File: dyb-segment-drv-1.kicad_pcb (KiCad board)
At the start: 2 copper layers, 76 x 76 mm, 192 parts, among them J1 Conn_01x10, Q1 HL2300, Q10 HL2300, Q11 HL2300, Q12 HL2300, Q13 HL2300, Q14 HL2300, Q15 HL2300, Q16 HL2300, Q2 HL2300, Q3 HL2300, Q4 HL2300, Q5 HL2300, Q6 HL2300, Q7 HL2300, Q8 HL2300, Q9 HL2300, SW1 SW_SPDT, U1 AP2112K-1.8, U10 74AUC2G32, U11 74AUC2G32, U12 74AUC2G32, U13 74AUC2G32, U14 74AUC2G32, U15 Inverter_Schmitt_Dual, U16 Inverter_Schmitt_Dual, U17 SN74AUP2G08, U18 SN74AUP2G08, U19 SN74AUP2G08, U2 GS3911AG, U20 SN74AUP2G08, U21 SN74AUP2G08, U22 74AUC2G32, U23 74AUC2G32, U24 74AUC2G32, U25 74AUC2G32, U26 74AUC2G32, U27 GS3911AG, U28 SN74AUP2G08, U29 SN74AUP2G08, U3 SN74AUP2G08, U30 SN74AUP2G08, U31 SN74AUP2G08, U32 SN74AUP2G08, U33 SN74AUP2G08, U34 74AUC2G32, U35 74AUC2G32, U36 74AUC2G32, U37 74AUC2G32, U38 74AUC2G32, U39 74AUC2G32, U4 SN74AUP2G08, U40 Inverter_Schmitt_Dual, U41 Inverter_Schmitt_Dual, U42 SN74AUP2G08, U43 SN74AUP2G08, U44 SN74AUP2G08, U45 SN74AUP2G08, U46 SN74AUP2G08, U47 74AUC2G32, U48 74AUC2G32, U49 74AUC2G32, U5 SN74AUP2G08, U50 74AUC2G32, U51 74AUC2G32, U6 SN74AUP2G08, U7 SN74AUP2G08, U8 SN74AUP2G08, U9 74AUC2G32

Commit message: pcb: add f routing
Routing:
- net /Segment Driver/~{D3}: track 110.0 -> 131.7 mm, vias 12 -> 17
- net /Segment Driver/~{D2}: track 81.4 -> 93.7 mm, vias 4 -> 8
- net Net-(U23-Pad3): track 0.00 -> 9.21 mm, vias 0 -> 2
- net Net-(U17-Pad3): track 0.00 -> 7.02 mm
- net /A2: track 85.7 -> 92.1 mm, vias 6 -> 8
- net /A0: track 69.6 -> 75.7 mm, vias 2 -> 4
- net /Segment Driver/~{D1}: track 90.5 -> 96.3 mm, vias 10 -> 12
- net Net-(U19-Pad7): track 0.00 -> 5.61 mm
- net Net-(U19-Pad3): track 0.00 -> 4.86 mm
- net Net-(U18-Pad7): track 0.00 -> 4.76 mm
- net Net-(U17-Pad7): track 0.00 -> 3.76 mm
- net Net-(U24-Pad6): track 0.00 -> 0.50 mm
- net GND: vias 0 -> 49

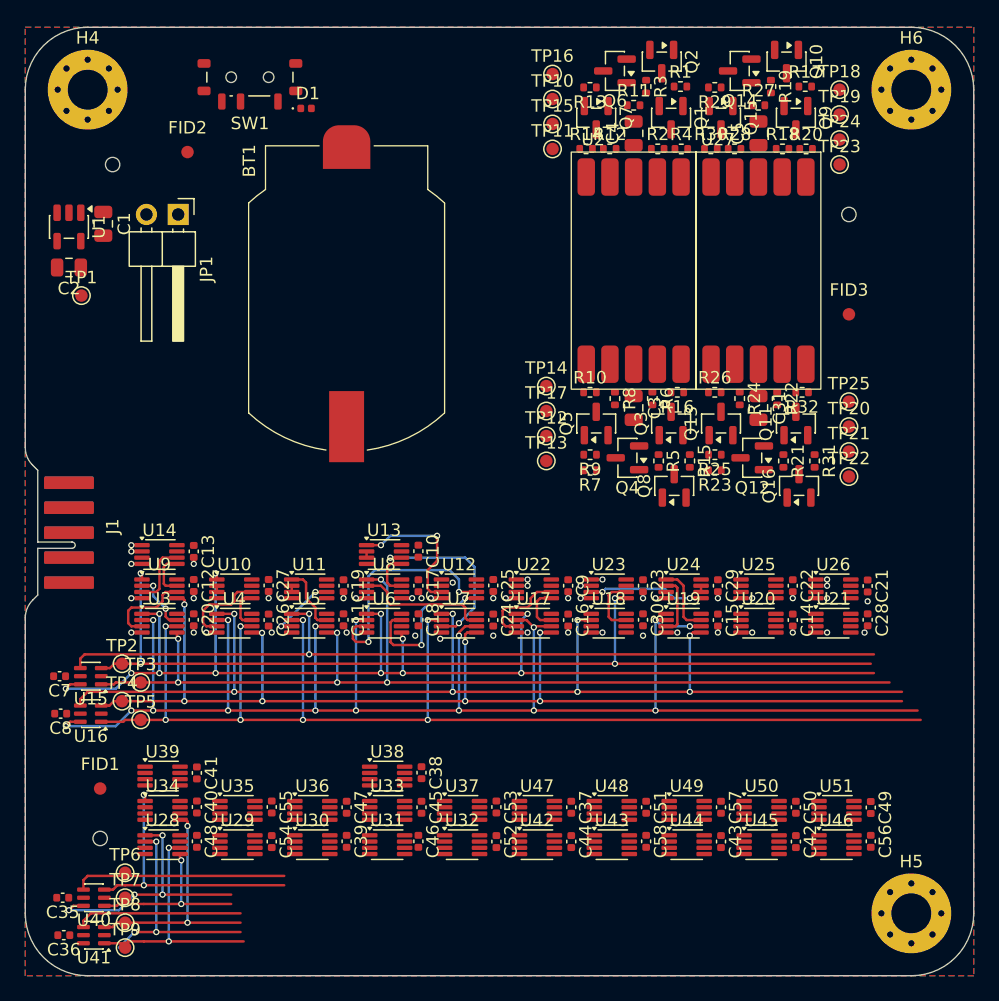
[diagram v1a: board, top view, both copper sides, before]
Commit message: pcb: route segments drivers
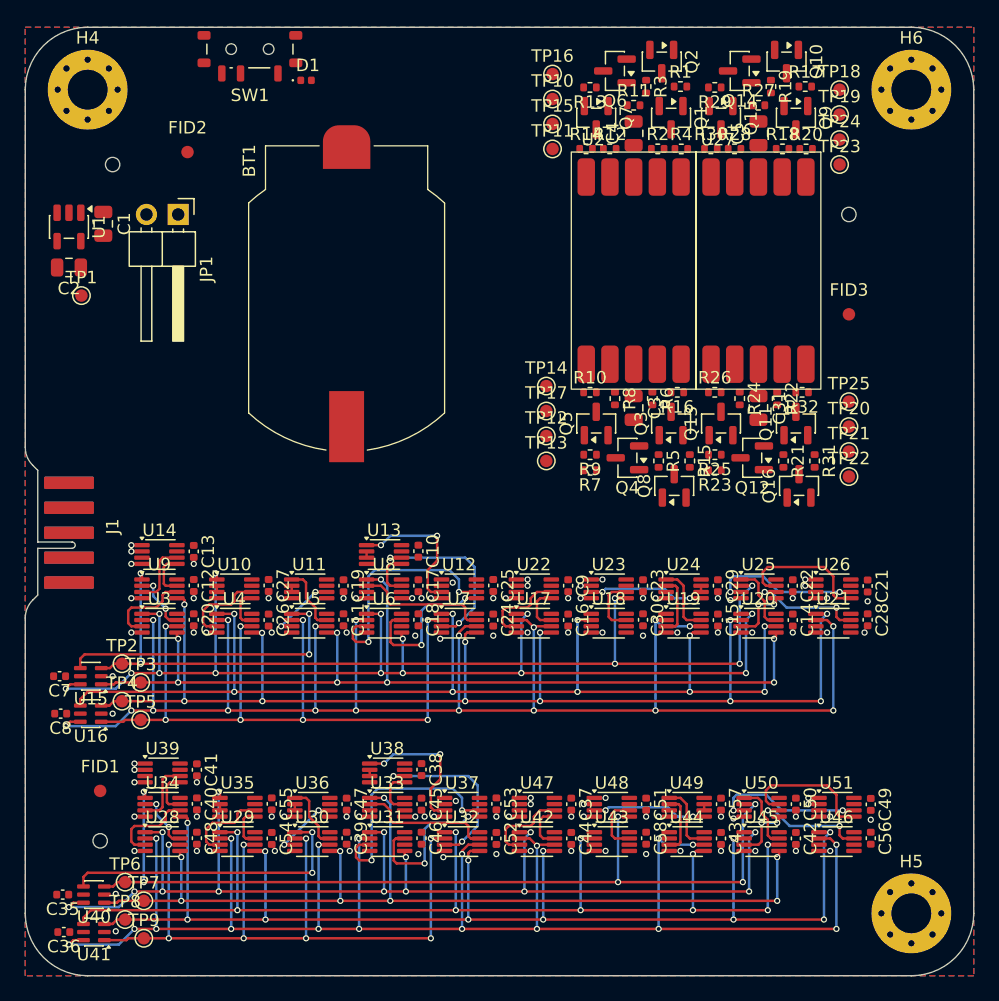
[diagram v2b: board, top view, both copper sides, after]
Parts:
- moved D1 2.25 mm to (132.5, 23.2)
- moved SW1 2.25 mm to (128.0, 20.8)
- moved TP9 1.68 mm to (119.5, 92.0)
- moved TP7 1.52 mm to (119.5, 89.0)
- moved TP6 0.75 mm to (118.0, 87.5)
- moved C46 0.35 mm to (141.8, 84.0)
- moved C35 0.25 mm to (113.0, 88.5)
- moved C36 0.25 mm to (113.1, 91.5)
- moved C37 0.25 mm to (153.8, 81.2)
- moved C38 0.25 mm to (141.8, 78.5)
- moved C39 0.25 mm to (135.8, 84.0)
- moved C40 0.25 mm to (123.8, 81.2)
- moved C41 0.25 mm to (123.8, 78.5)
- moved C42 0.25 mm to (171.8, 84.0)
- moved C43 0.25 mm to (165.8, 84.0)
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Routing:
- net /Segment Driver1/~{D3}: track 18.4 -> 133.3 mm, vias 3 -> 19
- net /B2: track 19.8 -> 101.1 mm, vias 2 -> 12
- net /Segment Driver1/~{D2}: track 13.3 -> 88.9 mm, vias 0 -> 10
- net /Segment Driver1/~{D1}: track 21.0 -> 91.9 mm, vias 4 -> 14
- net /B1: track 14.3 -> 76.5 mm, vias 2 -> 8
- net /B0: track 22.3 -> 72.8 mm, vias 2 -> 6
- net /Segment Driver/~{D0}: track 69.1 -> 23.9 mm
- net /B3: track 19.6 -> 61.0 mm, vias 2 -> 8
- net /A3: track 100.5 -> 61.0 mm
- net Net-(U31-Pad3): track 0.00 -> 18.7 mm, vias 0 -> 2
- net Net-(U32-Pad3): track 0.00 -> 14.5 mm, vias 0 -> 2
- net Net-(U31-Pad7): track 0.00 -> 12.7 mm, vias 0 -> 2
- net Net-(U50-Pad3): track 0.00 -> 12.1 mm, vias 0 -> 2
- net Net-(U25-Pad3): track 0.00 -> 12.1 mm, vias 0 -> 2
- net Net-(U37-Pad3): track 0.00 -> 11.7 mm, vias 0 -> 2
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
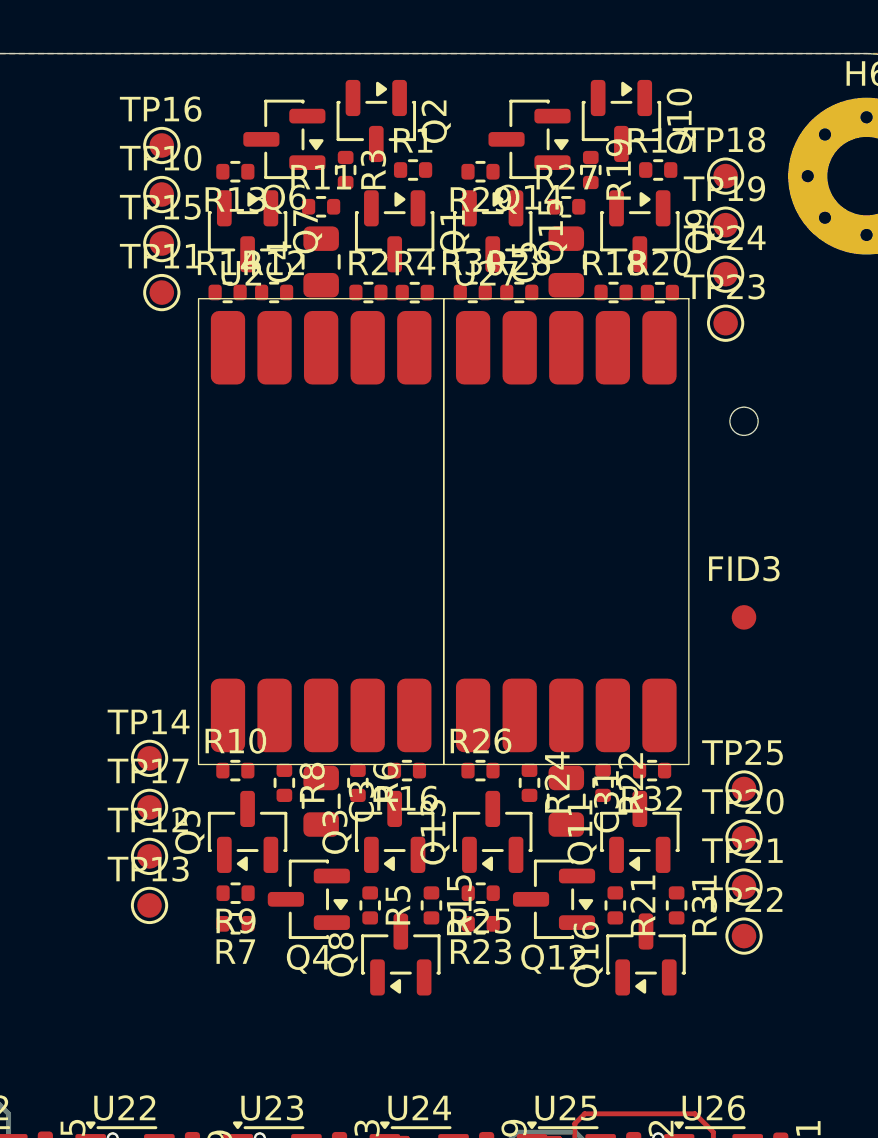
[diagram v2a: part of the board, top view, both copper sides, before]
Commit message: pcb: add segment shifters routing
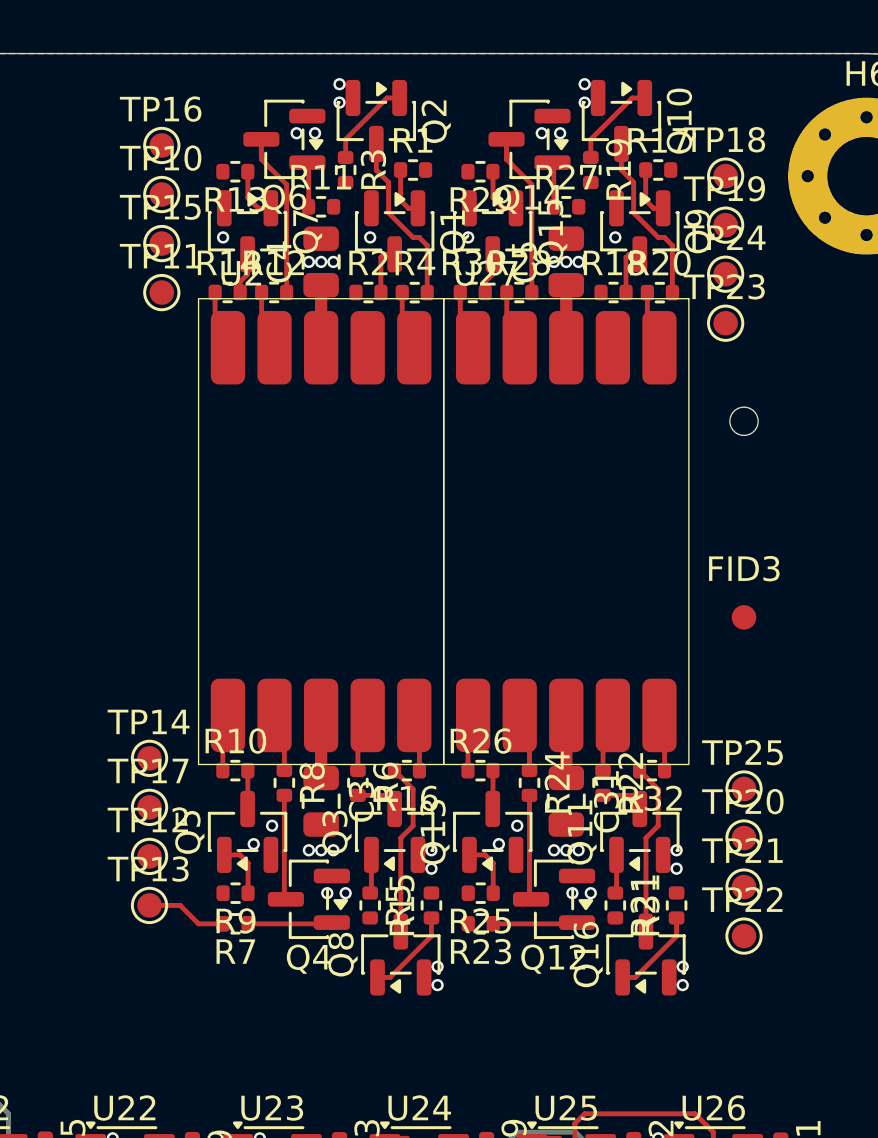
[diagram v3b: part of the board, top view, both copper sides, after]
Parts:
- turned R15 to 90 degrees
- turned R31 to 90 degrees
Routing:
- net +BATT: track 0.00 -> 10.2 mm
- net Net-(Q8-D): track 0.00 -> 7.08 mm
- net Net-(Q16-D): track 0.00 -> 7.08 mm
- net Net-(Q2-D): track 0.00 -> 7.07 mm
- net Net-(Q10-D): track 0.00 -> 7.07 mm
- net Net-(Q6-D): track 0.00 -> 6.67 mm
- net Net-(Q14-D): track 0.00 -> 6.67 mm
- net Net-(Q4-D): track 0.00 -> 4.27 mm
- net Net-(Q12-D): track 0.00 -> 4.27 mm
- net Net-(Q8-G): track 0.00 -> 3.64 mm
- net Net-(Q16-G): track 0.00 -> 3.64 mm
- net Net-(Q2-G): track 0.00 -> 3.64 mm
- net Net-(Q10-G): track 0.00 -> 3.64 mm
- net Net-(Q4-G): track 0.00 -> 3.44 mm
- net Net-(Q12-G): track 0.00 -> 3.44 mm
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
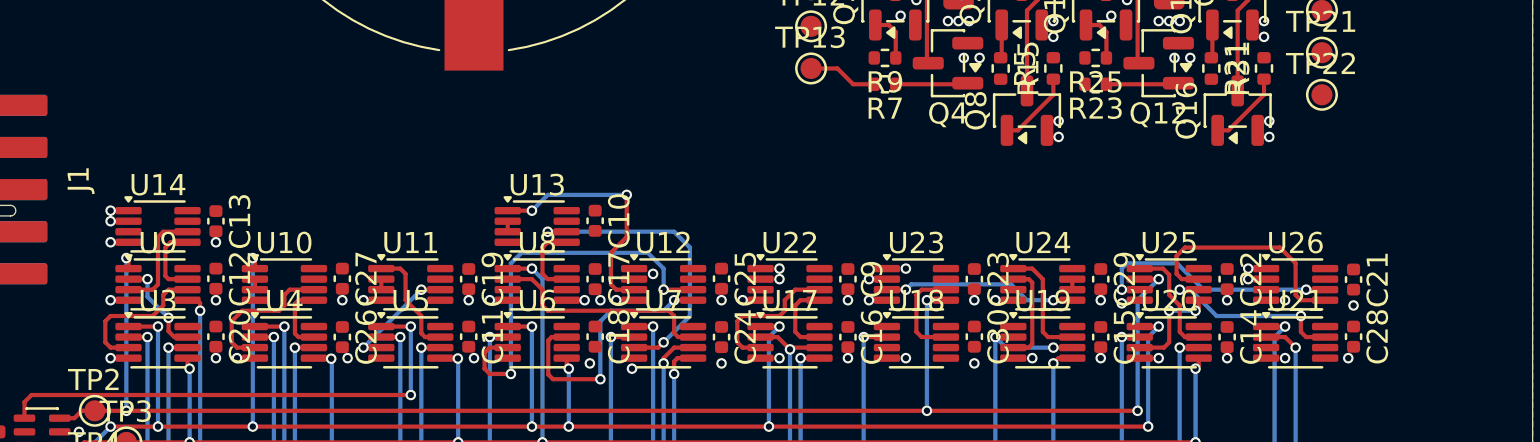
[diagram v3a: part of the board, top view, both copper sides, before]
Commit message: pcb: wrong segment routing
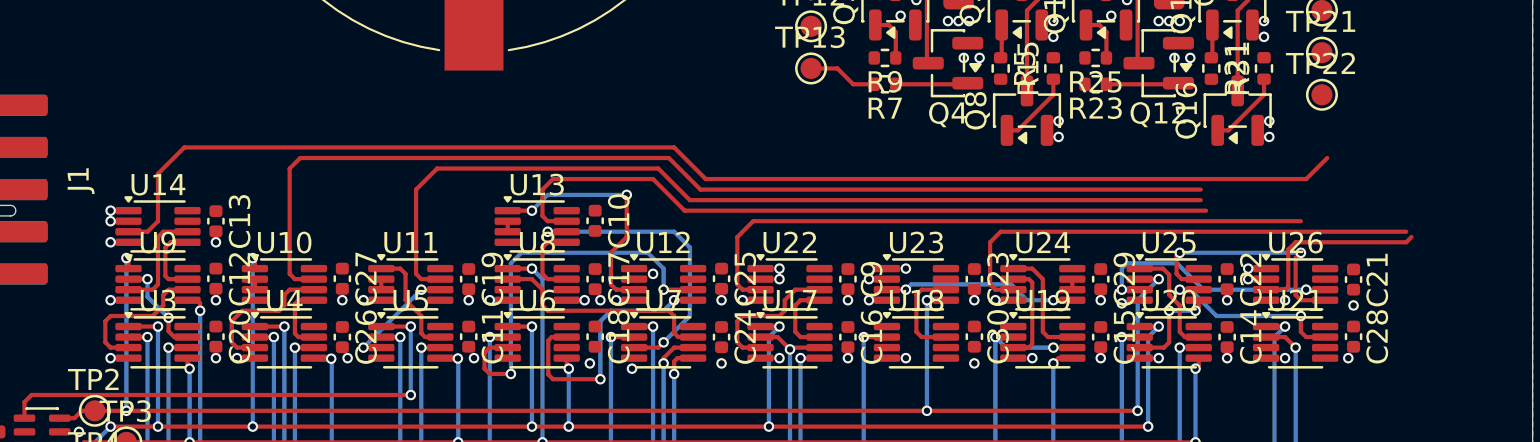
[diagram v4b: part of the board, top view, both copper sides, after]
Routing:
- net /Display/A: track 0.00 -> 60.9 mm
- net /Display/B: track 0.00 -> 50.3 mm
- net /Display/C: track 0.00 -> 43.5 mm
- net /Display/D: track 3.31 -> 38.1 mm
- net /Display/E: track 0.00 -> 30.5 mm
- net /Display/F: track 0.00 -> 23.2 mm
- net /Display/G: track 0.00 -> 8.96 mm
- net Net-(U25-Pad7): track 11.1 -> 11.6 mm, vias 0 -> 2

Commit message: pcb: route first number
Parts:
- moved TP14 6.50 mm to (151.8, 54.2)
- moved TP16 6.00 mm to (152.2, 28.8)
- moved TP11 4.00 mm to (152.2, 24.8), turned to 180 degrees
- moved TP10 2.00 mm to (152.2, 22.8), turned to 180 degrees
- moved TP12 1.50 mm to (151.8, 50.2)
- moved TP13 1.50 mm to (151.8, 52.2)
- moved TP17 1.50 mm to (151.8, 48.2)
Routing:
- net /Display/G: track 8.96 -> 58.8 mm, vias 0 -> 2
- net /Display/F: track 23.2 -> 48.3 mm, vias 0 -> 2
- net /Display/D: track 38.1 -> 20.0 mm
- net /Display/E: track 30.5 -> 12.4 mm
- net /Display/C: track 43.5 -> 30.5 mm
- net /Display/B: track 50.3 -> 62.9 mm
- net /Display/A: track 60.9 -> 69.0 mm

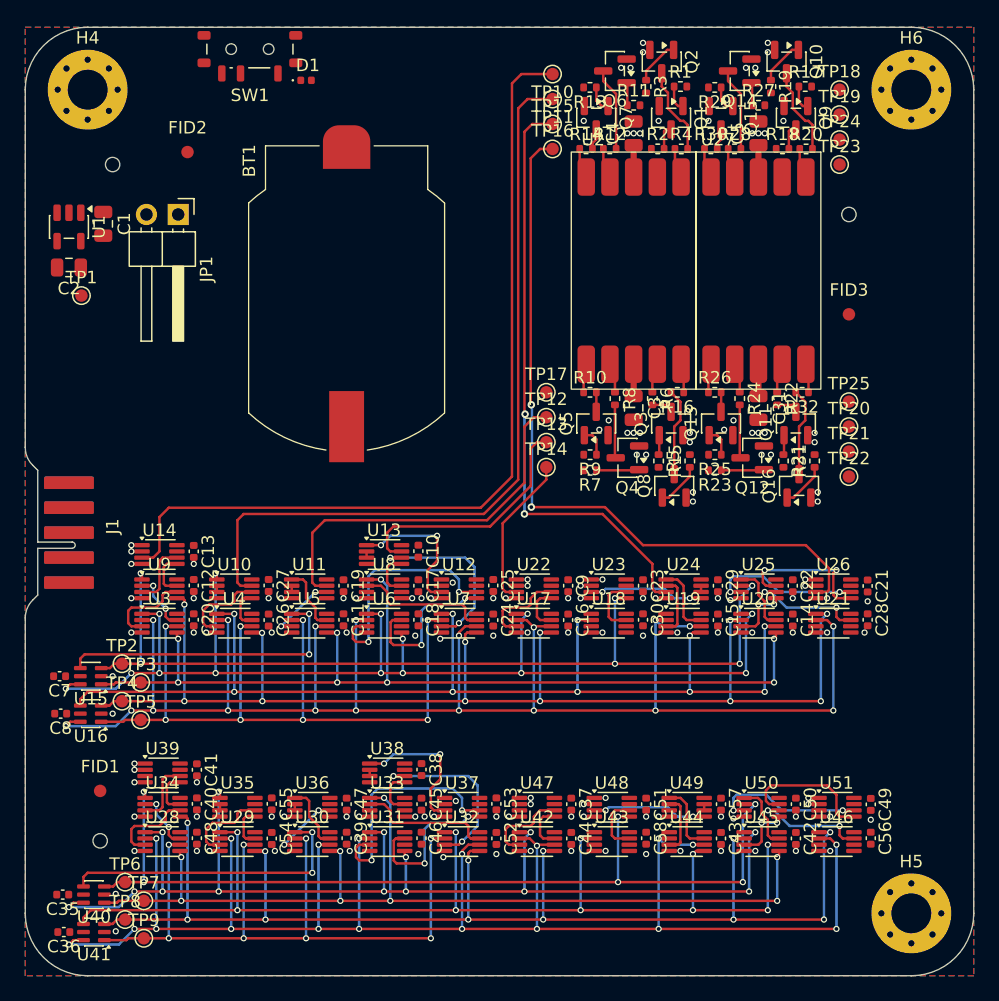
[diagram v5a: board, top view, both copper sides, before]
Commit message: pcb: add second digit routing
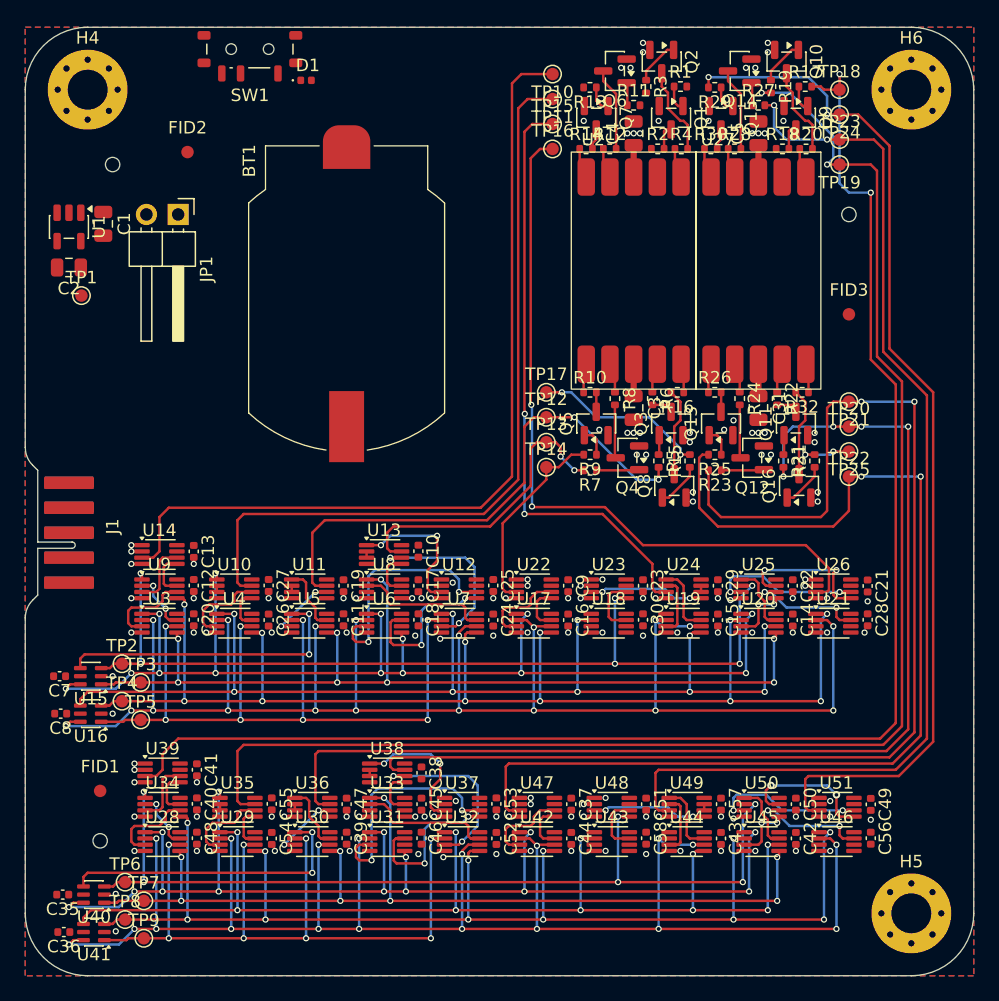
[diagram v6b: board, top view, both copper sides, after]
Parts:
- moved TP19 4.00 mm to (175.2, 30.0), turned to 180 degrees
- moved TP21 4.00 mm to (176.0, 49.0), turned to 180 degrees
- moved TP25 4.00 mm to (176.0, 53.0), turned to 180 degrees
- moved TP23 2.00 mm to (175.2, 28.0)
- moved TP24 2.00 mm to (175.2, 26.0), turned to 180 degrees
- moved C38 0.27 mm to (141.8, 78.8)
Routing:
- net /Display1/A: track 0.00 -> 121.1 mm, vias 0 -> 2
- net /Display1/B: track 0.00 -> 119.5 mm, vias 0 -> 2
- net /Display1/D: track 0.00 -> 99.5 mm, vias 0 -> 2
- net /Display1/C: track 0.00 -> 91.9 mm, vias 0 -> 4
- net /Display1/F: track 0.00 -> 87.5 mm, vias 0 -> 2
- net /Display1/E: track 0.00 -> 86.0 mm, vias 0 -> 2
- net /Display1/G: track 0.00 -> 82.6 mm, vias 0 -> 2
- net /Display/DP: track 0.00 -> 13.9 mm, vias 0 -> 2
- net /Display/C: track 30.5 -> 42.5 mm, vias 0 -> 2
- net /Display/D: track 20.0 -> 24.4 mm, vias 0 -> 2
- net /Display1/DP: track 0.00 -> 4.36 mm, vias 0 -> 2
- net /Display/E: track 12.4 -> 15.8 mm
- net Net-(U50-Pad7): vias 0 -> 2
- net GND: vias 141 -> 139
